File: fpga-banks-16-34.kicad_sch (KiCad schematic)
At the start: 25 parts, among them U1 ASFLMB-100.000MHZ-XY-T, U15 XC7K160T-FFG676, U8 PCA9517ADMR2G

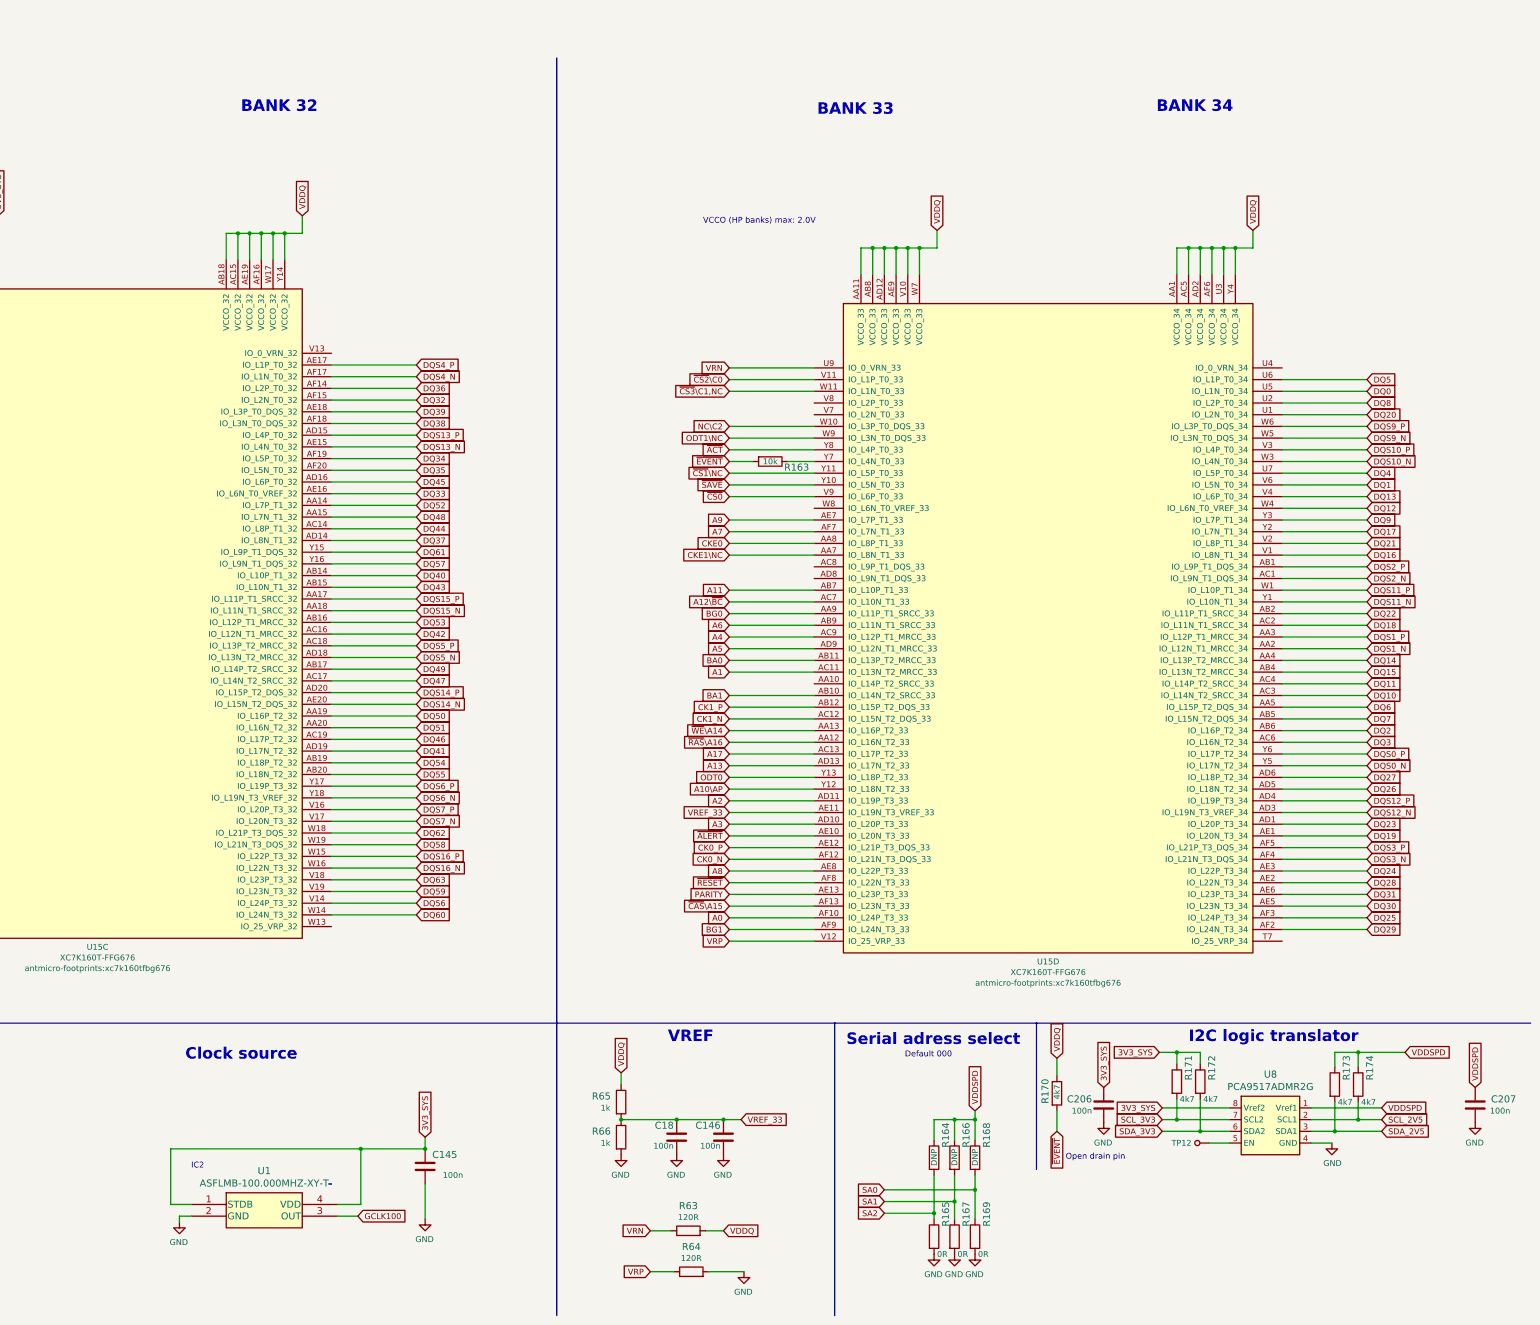
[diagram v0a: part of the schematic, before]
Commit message: replace 120R VRN, VRP resistors with 80.6R ones
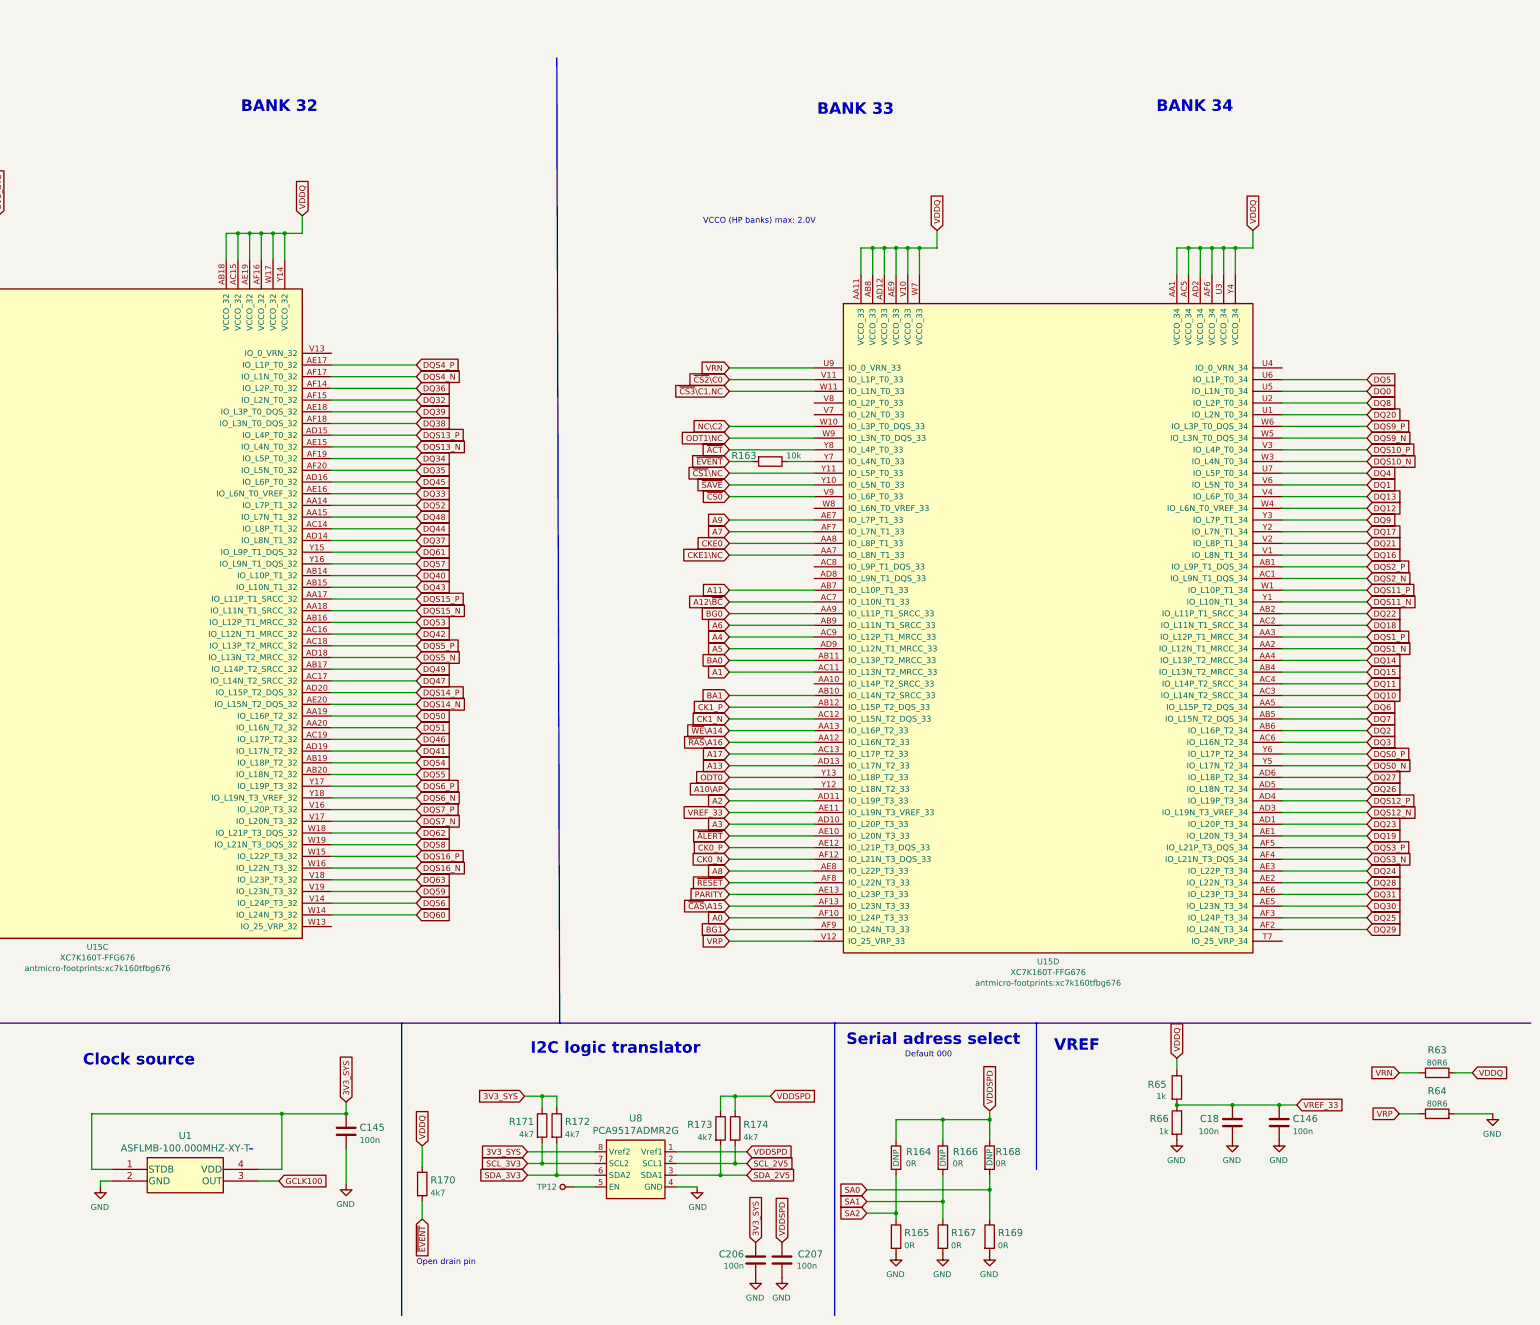
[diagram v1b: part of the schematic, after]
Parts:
- removed R63, R64: R_120R_0603, data-center-dram-tester-footprints:0603-res, symbol data-center-dram-tester:R_120R_0603
- added R63, R64: R_80R6_0603, antmicro-footprints:0603-res, symbol antmicroResistors0603:R_80R6_0603
- R164, R166, R168: Val (none) -> 0R
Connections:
- net GND: now also R64.2
- net VDDQ: now also R63.2
- net VRN: now also R63.1
- net VRP: now also R64.1
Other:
- note removed: "IC2"
- moved on the sheet: C145, C146, C18, C206, C207, R164, R165, R166, R167, R168, R169, R170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

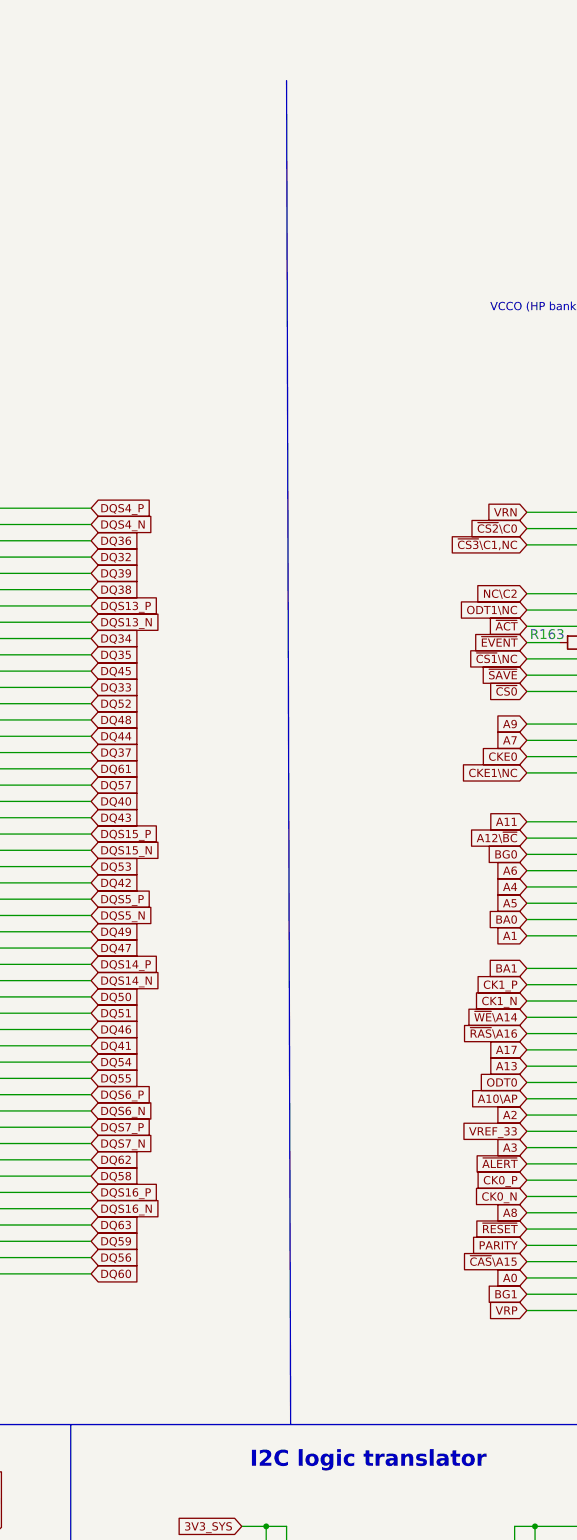
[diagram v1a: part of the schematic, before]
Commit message: Progress in HS matching and deskewing, clear DRC, implement schematic review changes, SI improvments
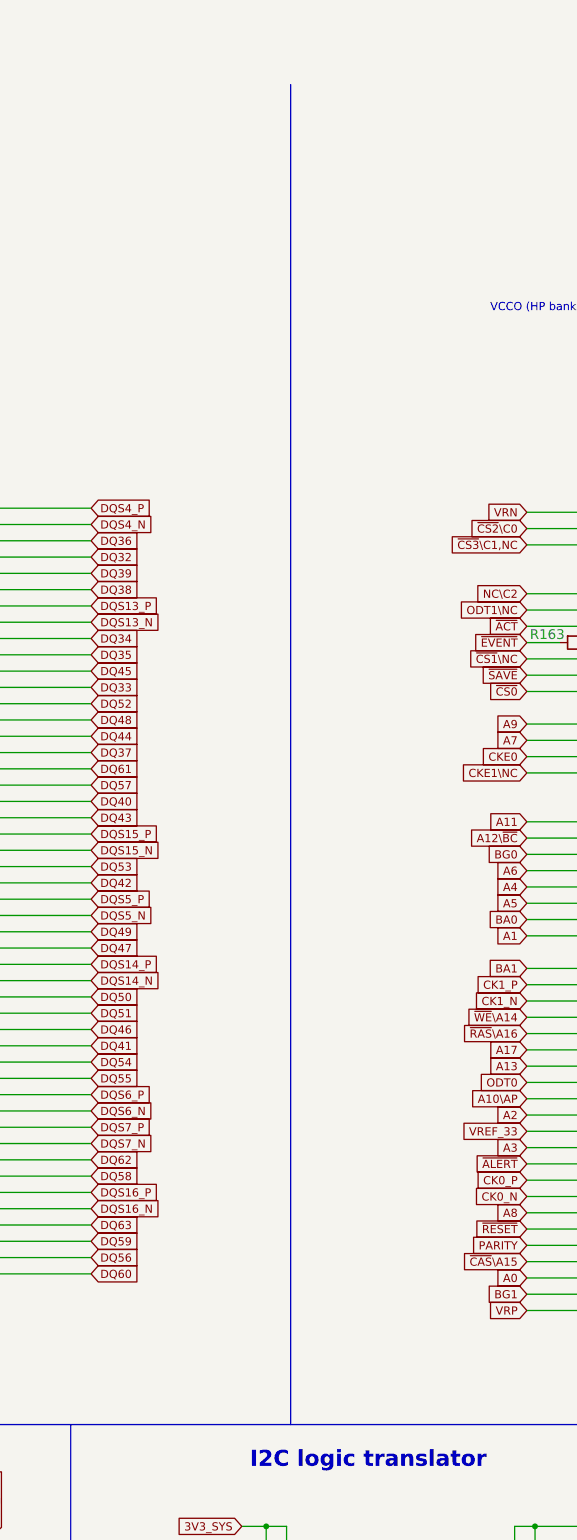
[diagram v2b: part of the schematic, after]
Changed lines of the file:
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@@
     (stroke (width 0) (type default) (color 0 0 0 0))
   )
-  (polyline (pts (xy 196.215 12.065) (xy 196.85 221.615))
+  (polyline (pts (xy 196.85 12.7) (xy 196.85 221.615))
     (stroke (width 0) (type default) (color 0 0 0 0))
   )

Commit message: SI improvments
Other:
- note removed: "TODO: VRN, VRL to 80Ohm"
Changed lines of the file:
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@@
     (effects (font (size 2.4892 2.4892) (thickness 0.4978) bold) (justify left bottom))
-  )
-  (text "TODO: VRN, VRL to 80Ohm\n" (at 1.905 3.81 0)
-    (effects (font (size 1.27 1.27)) (justify left bottom))
   )
   (global_label "DQ51" (shape input) (at 165.735 157.48 0) (fields_autoplaced)

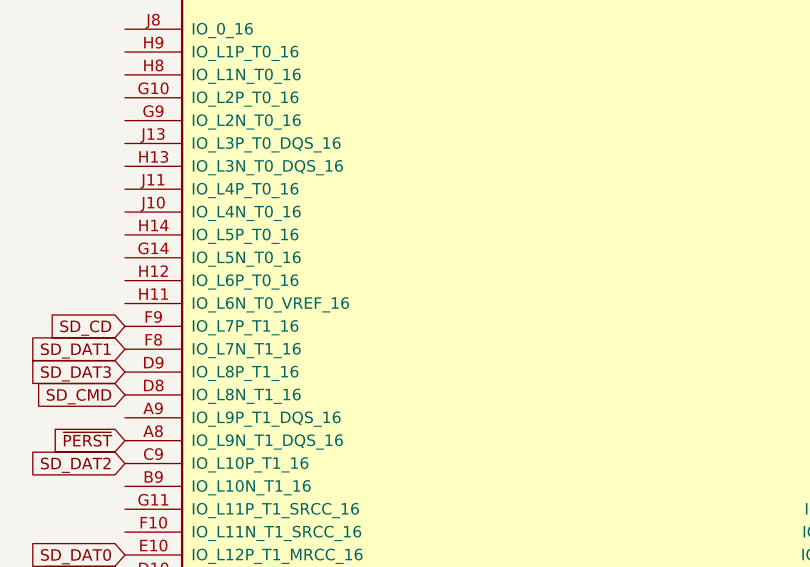
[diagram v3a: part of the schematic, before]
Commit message: Optimize BOM, add all bank 115 and 116 REFCLK's to FMC connector
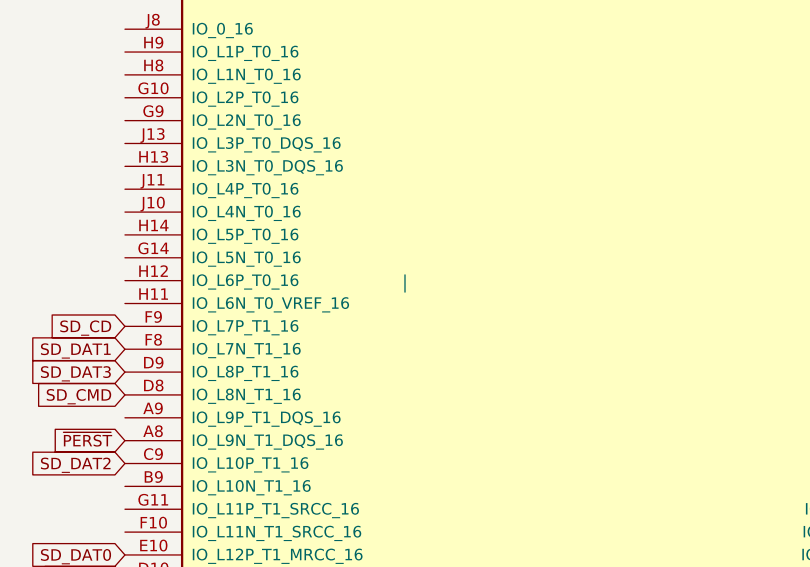
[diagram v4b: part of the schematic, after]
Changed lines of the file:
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@@
+    (stroke (width 0) (type default) (color 0 0 0 0))
+  )
+  (wire (pts (xy 76.835 105.41) (xy 76.835 103.505))
     (stroke (width 0) (type default) (color 0 0 0 0))
   )
